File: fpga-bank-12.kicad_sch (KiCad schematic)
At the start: 1 part

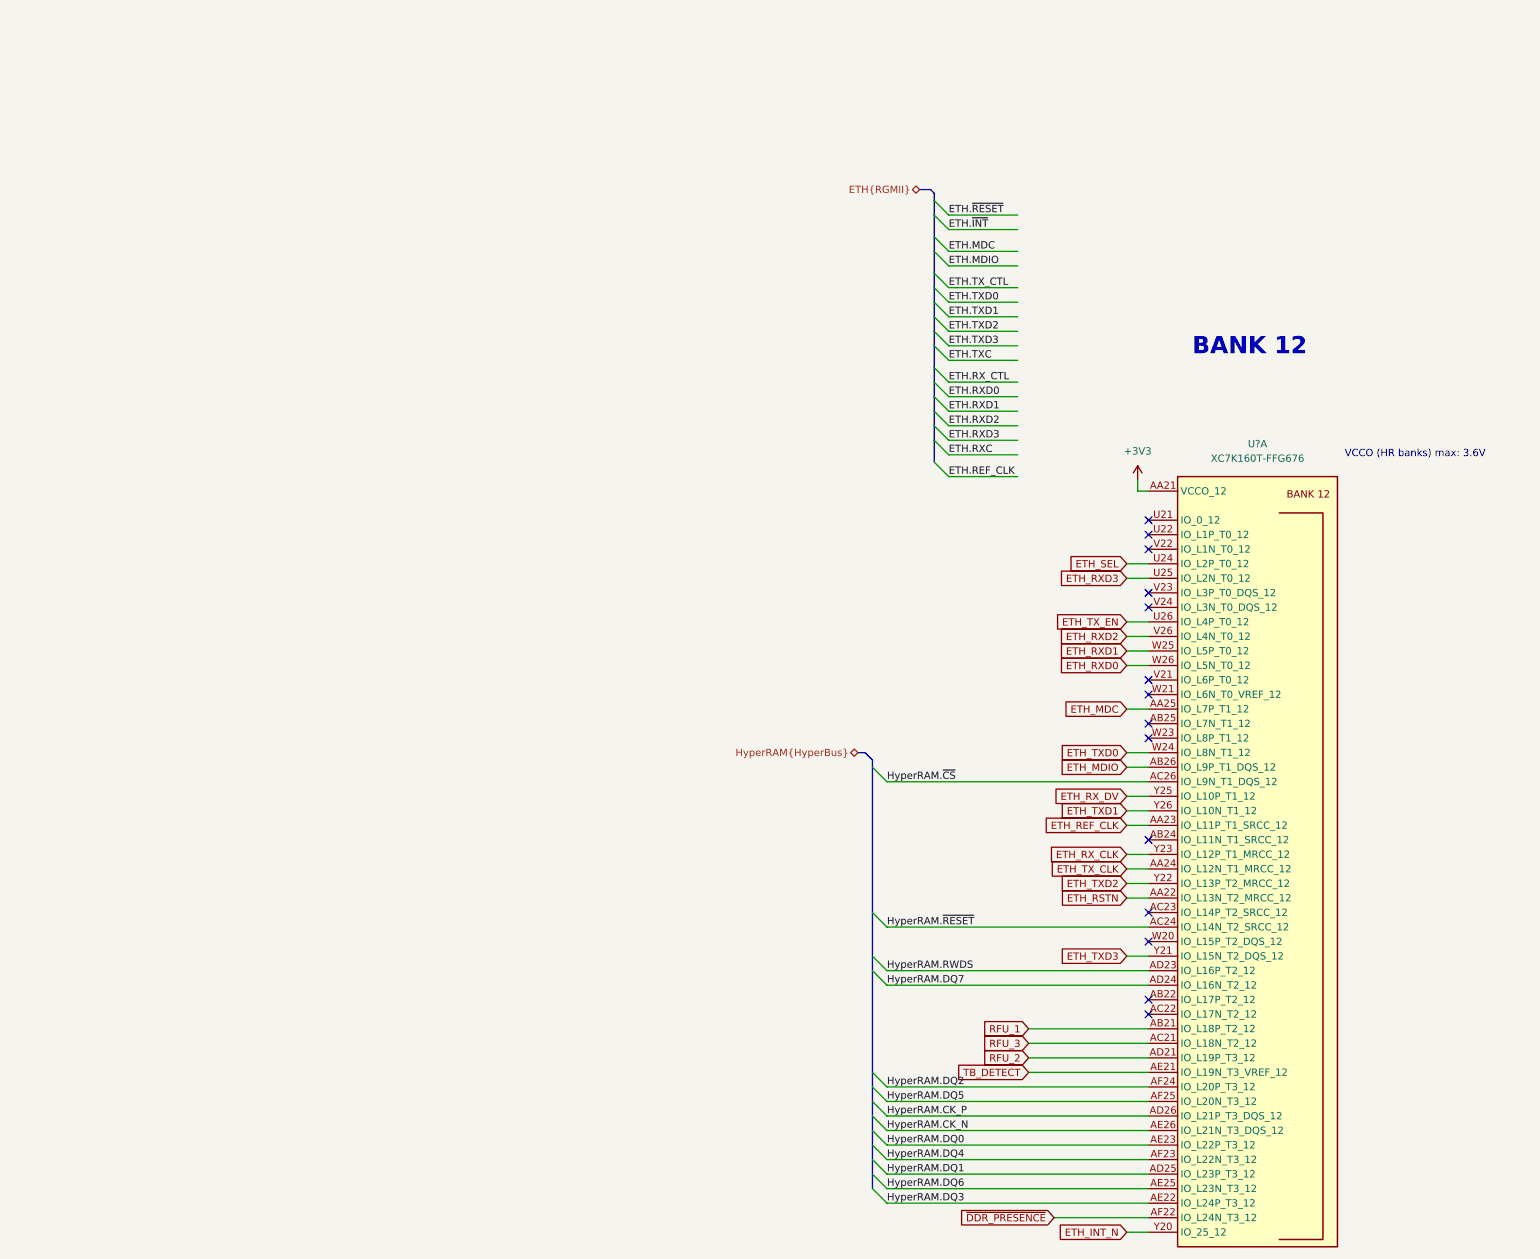
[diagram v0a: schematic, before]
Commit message: Finish reconnecting signals after migration to the hierarchical structure
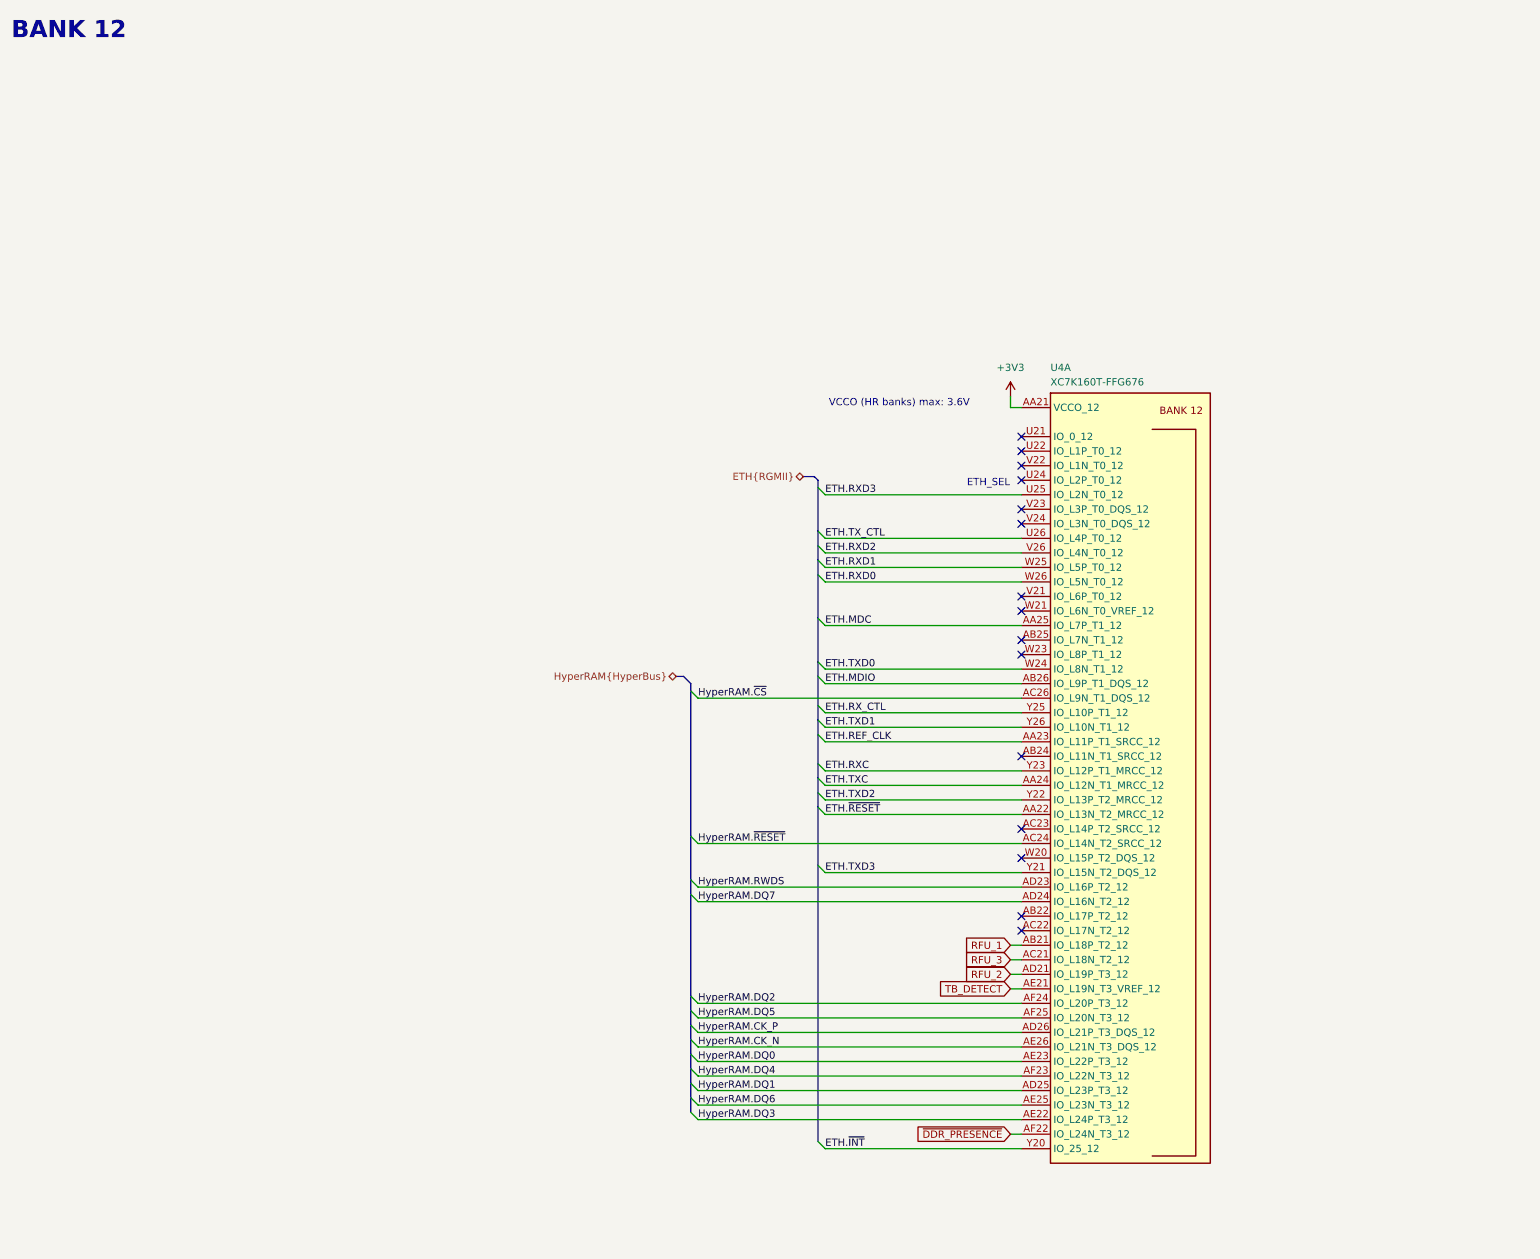
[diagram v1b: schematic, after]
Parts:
- gave numbers to parts that had none: 1
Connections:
- net ETH_INT_N is gone; now on net ETH.~{INT}: U4.Y20 (IO_25_12)
- net ETH_MDC is gone; now on net ETH.MDC: U4.AA25 (IO_L7P_T1_12)
- net ETH_MDIO is gone; now on net ETH.MDIO: U4.AB26 (IO_L9P_T1_DQS_12)
- net ETH_REF_CLK is gone; now on net ETH.REF_CLK: U4.AA23 (IO_L11P_T1_SRCC_12)
- net ETH_RSTN is gone; now on net ETH.~{RESET}: U4.AA22 (IO_L13N_T2_MRCC_12)
- net ETH_RXD0 is gone; now on net ETH.RXD0: U4.W26 (IO_L5N_T0_12)
- net ETH_RXD1 is gone; now on net ETH.RXD1: U4.W25 (IO_L5P_T0_12)
- net ETH_RXD2 is gone; now on net ETH.RXD2: U4.V26 (IO_L4N_T0_12)
- net ETH_RXD3 is gone; now on net ETH.RXD3: U4.U25 (IO_L2N_T0_12)
- net ETH_RX_CLK is gone; now on net ETH.RXC: U4.Y23 (IO_L12P_T1_MRCC_12)
- net ETH_RX_DV is gone; now on net ETH.RX_CTL: U4.Y25 (IO_L10P_T1_12)
- net ETH_TXD0 is gone; now on net ETH.TXD0: U4.W24 (IO_L8N_T1_12)
- net ETH_TXD1 is gone; now on net ETH.TXD1: U4.Y26 (IO_L10N_T1_12)
- net ETH_TXD2 is gone; now on net ETH.TXD2: U4.Y22 (IO_L13P_T2_MRCC_12)
- net ETH_TXD3 is gone; now on net ETH.TXD3: U4.Y21 (IO_L15N_T2_DQS_12)
- net ETH_TX_CLK is gone; now on net ETH.TXC: U4.AA24 (IO_L12N_T1_MRCC_12)
- net ETH_TX_EN is gone; now on net ETH.TX_CTL: U4.U26 (IO_L4P_T0_12)
- net ETH_SEL: no longer names the net of U4.U24 (IO_L2P_T0_12)
- no-connect marks 14 -> 15
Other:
- note added: "ETH_SEL"
- moved on the sheet: U4A

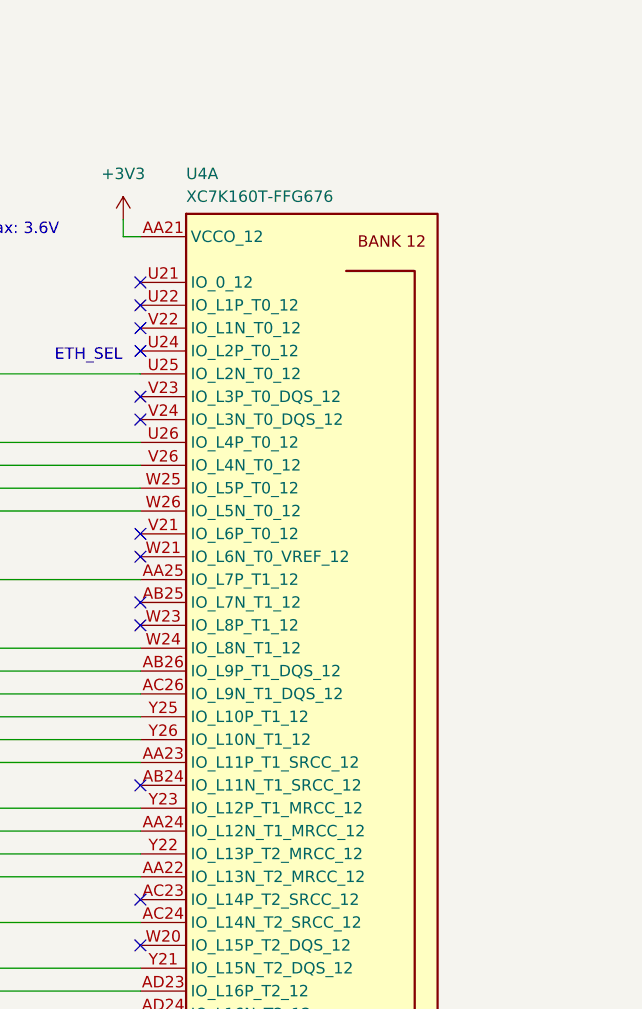
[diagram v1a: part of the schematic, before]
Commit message: Fix FPGA properties from the standardized library, update SO-DIMM symbol
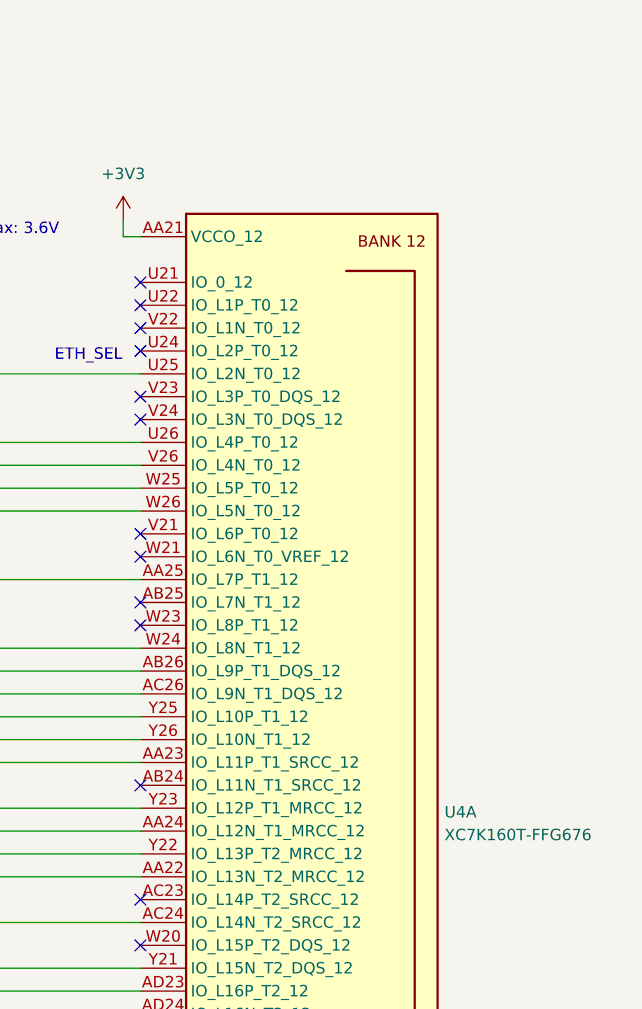
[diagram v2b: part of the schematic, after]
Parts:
- U4: footprint sodimm-ddr5-tester-footprints:BGA-676_27x27mm_Layout26x26_P1X1mm -> antmicro-footprints:BGA-676_27x27mm_Layout26x26_P1X1mm; symbol sodimm-ddr5-tester:XC7K160T-FFG676 -> antmicroMicrocontrollers:XC7K160T-FFG676; Manufacturer Xilinx -> AMD-Xilinx
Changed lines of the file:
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@@
     (pin "1")
   )
-  (symbol (lib_id "sodimm-ddr5-tester:XC7K160T-FFG676") (at 191.77 83.82 0) (unit 1)
-    (in_bom yes) (on_board yes)
-    (property "Reference" "U4" (id 0) (at 196.85 76.835 0)
+  (symbol (lib_id "antmicroMicrocontrollers:XC7K160T-FFG676") (at 191.77 83.82 0) (unit 1)
+    (in_bom yes) (on_board yes) (fields_autoplaced)
+    (property "Reference" "U4" (id 0) (at 225.552 147.7594 0)
       (effects (font (size 1.27 1.27)) (justify left))
     )
-    (property "Value" "XC7K160T-FFG676" (id 1) (at 196.85 79.3653 0)
+    (property "Value" "XC7K160T-FFG676" (id 1) (at 225.552 150.2897 0)
       (effects (font (size 1.27 1.27) (thickness 0.15)) (justify left))
     )
-    (property "Footprint" "sodimm-ddr5-tester-footprints:BGA-676_27x27mm_Layout26x26_P1X1mm" (id 2) (at 260.35 86.36 0)
+    (property "Footprint" "antmicro-footprints:BGA-676_27x27mm_Layout26x26_P1X1mm" (id 2) (at 260.35 86.36 0)
       (effects (font (size 1.27 1.27) (thickness 0.15)) (justify left bottom) hide)
     )
@@
       (effects (font (size 1.27 1.27) (thickness 0.15)) (justify left bottom) hide)
     )
-    (property "Manufacturer" "Xilinx" (id 7) (at 191.77 83.82 0)
+    (property "Manufacturer" "AMD-Xilinx" (id 7) (at 191.77 83.82 0)
       (effects (font (size 1.27 1.27)) hide)
     )

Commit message: Loclib of the project
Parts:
- U4: footprint antmicro-footprints:BGA-676_27x27mm_Layout26x26_P1X1mm -> sodimm-ddr5-tester-footprints:BGA-676_27x27mm_Layout26x26_P1X1mm; symbol antmicroMicrocontrollers:XC7K160T-FFG676 -> sodimm-ddr5-tester:XC7K160T-FFG676

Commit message: Clean schematic DRC
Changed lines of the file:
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@@
     (effects (font (size 1.27 1.27)) (justify right))
   )
-  (symbol (lib_id "sodimm-ddr5-tester:+3V3") (at 189.865 81.915 0) (unit 1)
+  (symbol (lib_id "power:+3V3") (at 189.865 81.915 0) (unit 1)
     (in_bom yes) (on_board yes) (fields_autoplaced)
     (property "Reference" "#PWR0425" (id 0) (at 189.865 85.725 0)
       (effects (font (size 1.27 1.27)) hide)
     )
-    (property "Value" "+3V3" (id 1) (at 189.865 76.835 0))
-    (property "Footprint" "" (id 2) (at 189.865 81.915 0)
-      (effects (font (size 1.27 1.27)) hide)
+    (property "Value" "+3V3" (id 1) (at 186.69 79.375 0)
+      (effects (font (size 1.27 1.27) (thickness 0.15)) (justify left bottom))
     )
-    (property "Datasheet" "" (id 3) (at 189.865 81.915 0)
-      (effects (font (size 1.27 1.27)) hide)
+    (property "Footprint" "" (id 2) (at 205.105 89.535 0)
+      (effects (font (size 1.27 1.27) (thickness 0.15)) (justify left bottom) hide)
+    )
+    (property "Datasheet" "" (id 3) (at 205.105 92.075 0)
+      (effects (font (size 1.27 1.27) (thickness 0.15)) (justify left bottom) hide)
+    )
+    (property "Author" "Antmicro" (id 4) (at 205.105 84.455 0)
+      (effects (font (size 1.27 1.27) (thickness 0.15)) (justify left bottom) hide)
+    )
+    (property "License" "Apache-2.0" (id 5) (at 205.105 86.995 0)
+      (effects (font (size 1.27 1.27) (thickness 0.15)) (justify left bottom) hide)
     )
     (pin "1")

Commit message: [#57478] ohp release
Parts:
- U4: footprint sodimm-ddr5-tester-footprints:BGA-676_27x27mm_Layout26x26_P1X1mm -> antmicro-footprints:BGA-676_27x27mm_Layout26x26_P1x1mm_FFG676; symbol sodimm-ddr5-tester:XC7K160T-FFG676 -> antmicroFPGAChips:XC7K160T-FFG676
